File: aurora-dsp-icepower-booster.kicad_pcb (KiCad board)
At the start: 2 copper layers, 200 x 200 mm, 243 parts, among them J1 XLR_IN_1, J10 XLR3_OUT, J11 XLR3_OUT, J12 XLR3_OUT, J13 24V DC, J14 REMOTE 3.5mm, J2 XLR_IN_2, J3 XLR_IN_3, J4 XLR_IN_4, J5 XLR_IN_5, J6 XLR_IN_6, J7 XLR3_OUT, J8 XLR3_OUT, J9 XLR3_OUT, SW1 Gain CH1, SW2 Gain CH2, SW3 Gain CH3, SW4 Gain CH4, SW5 Gain CH5, SW6 Gain CH6, SW7 ALWAYS/REMOTE, U1 LM4562, U10 LM4562, U11 LM4562, U12 LM4562, U13 TEL5-2422, U14 ADP7118ARDZ-11, U15 ADP7182AUJZ-11, U2 LM4562, U3 LM4562, U4 LM4562, U5 LM4562, U6 LM4562, U7 LM4562, U8 LM4562, U9 LM4562

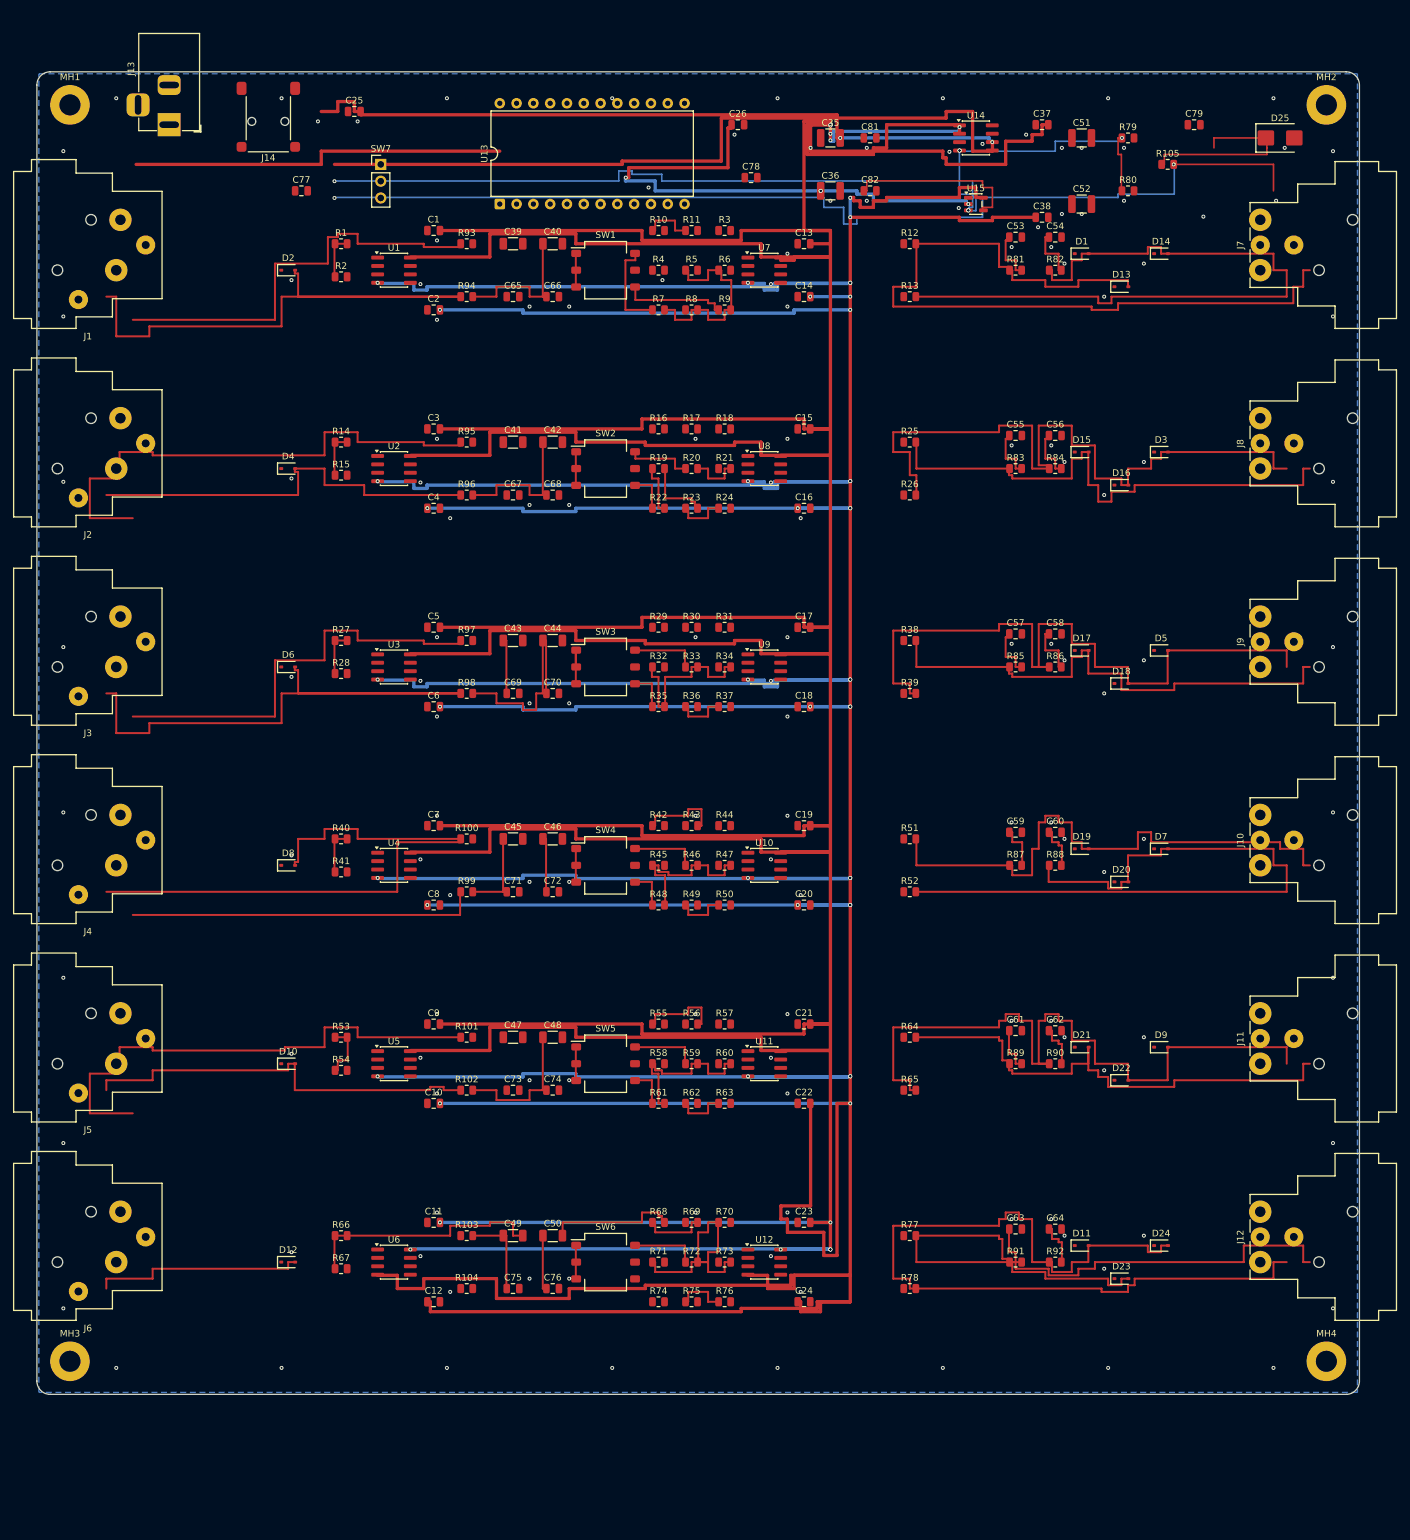
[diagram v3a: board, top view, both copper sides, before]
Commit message: SW7: Pin Header -> EG1224 SPDT Rocker Switch, Board 200x220mm, J13/SW7/J14 zentriert
- SW7 Footprint: PinHeader_1x03 -> SW_E-Switch_EG1224_SPDT_Angled
- SW7 rotiert 180°, ragt 10mm über Oberkante hinaus (Kippschalter)
- J13 (Barrel Jack) bei x=80, ragt 9mm über Oberkante
- J14 (3.5mm Remote) bei x=120, ragt 4.5mm über Oberkante
- Board von 200x200mm auf 200x220mm vergrößert (+20mm Y)
- Alle Bauteile 10mm nach unten verschoben (mehr Platz für PSU-Bereich)
- XLR IN/OUT: y=40..190 (vorher y=30..180)
- U13 (TEL5-2422) bei (70,30), PSU-Passives neu platziert
- Mounting Holes an neuen Ecken (5,5)(195,5)(5,215)(195,215)
- ERC: 805 Warnungen (Baseline, keine neuen Fehler)
- Schaltplan Footprint-Property ebenfalls aktualisiert
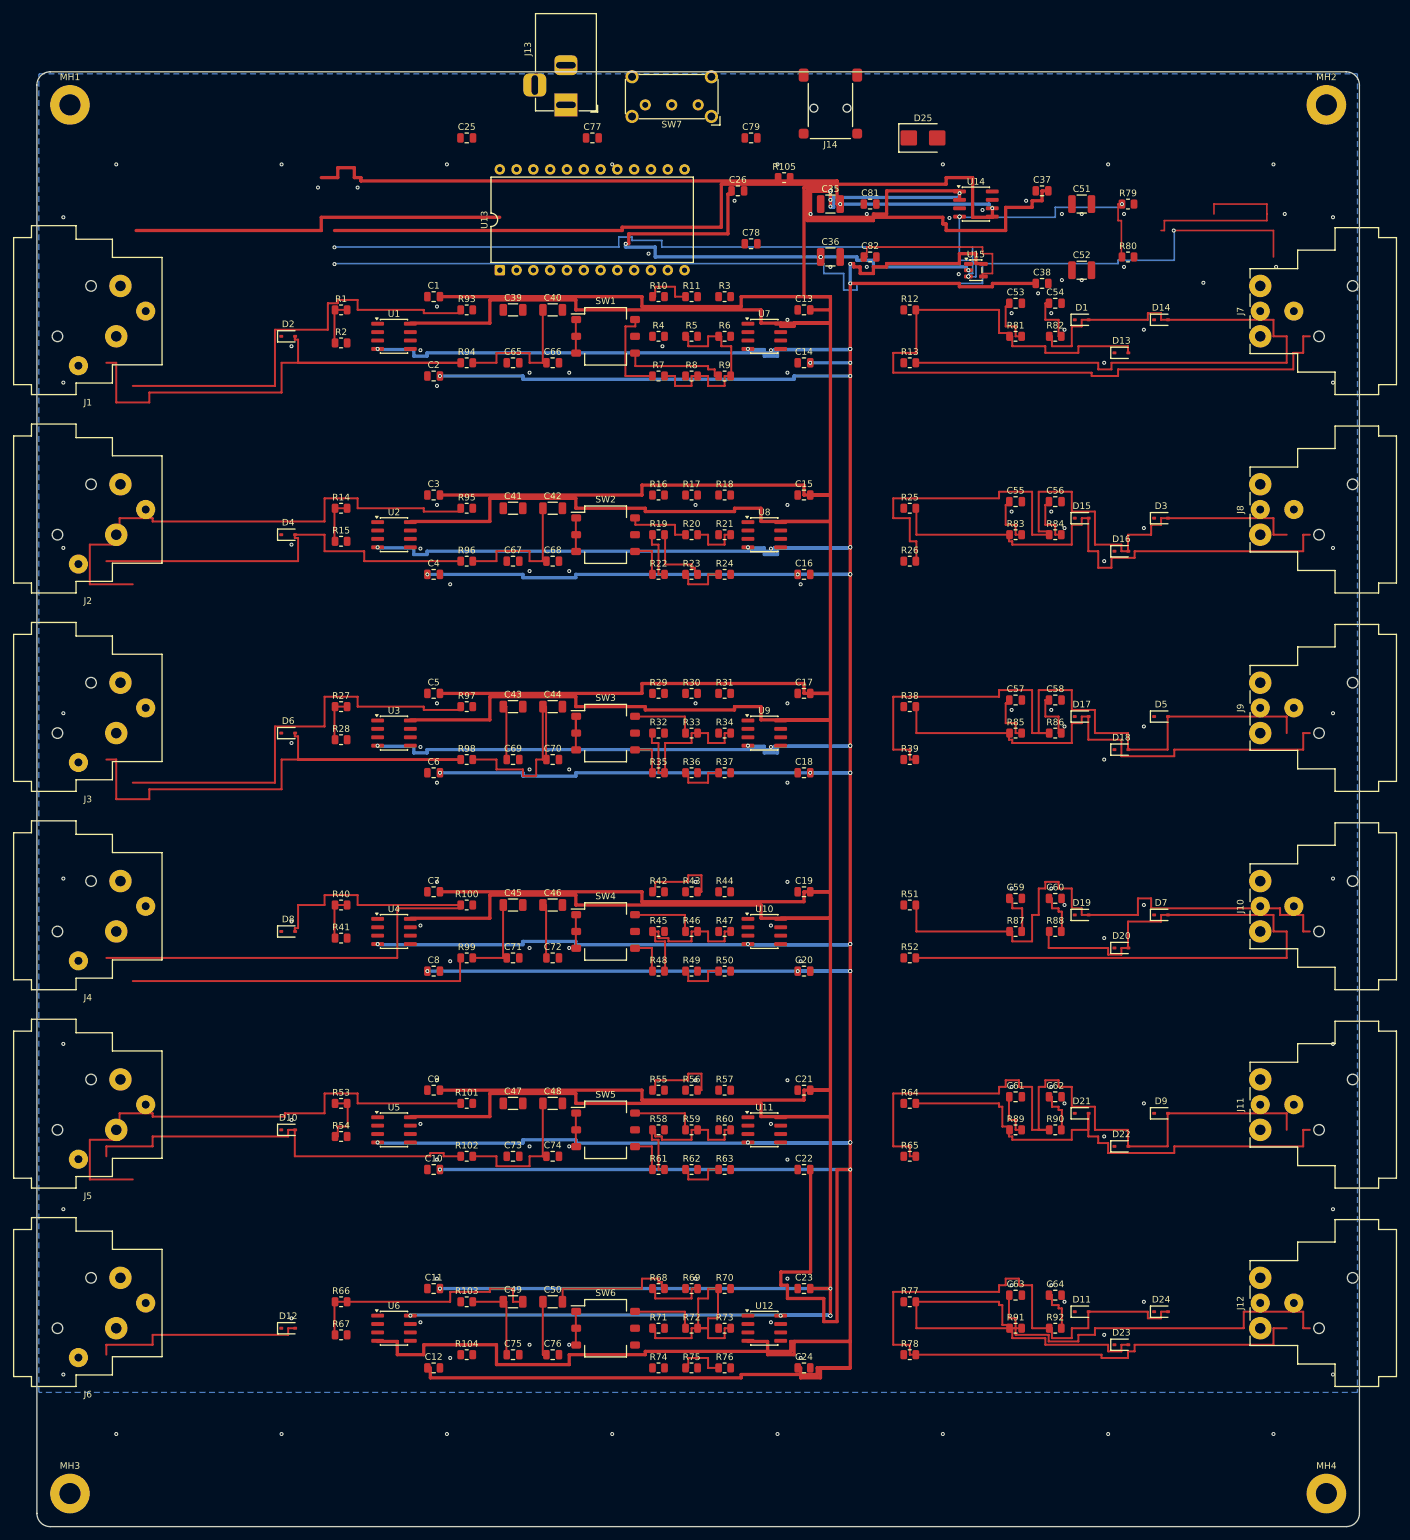
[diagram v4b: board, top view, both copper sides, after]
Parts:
- SW7: footprint Connector_PinHeader_2.54mm:PinHeader_1x03_P2.54mm_Vertical -> SW_E-Switch_EG1224_SPDT_Angled
- moved J14 85.0 mm to (120.0, 3.00)
- moved C79 67.0 mm to (108.0, 10.0)
- moved J13 60.1 mm to (80.0, 5.00)
- moved R105 58.0 mm to (113.0, 16.0)
- moved D25 54.0 mm to (134.0, 10.0)
- moved SW7 48.8 mm to (100.0, 5.00), turned to 180 degrees
- moved C77 44.7 mm to (84.0, 10.0)
- moved MH3 20.0 mm to (5.00, 215.0)
- moved MH4 20.0 mm to (195.0, 215.0)
- moved C25 17.5 mm to (65.0, 10.0)
- moved C1 10.0 mm to (60.0, 34.0)
- moved C10 10.0 mm to (60.0, 166.0)
- moved C11 10.0 mm to (60.0, 184.0)
- moved C12 10.0 mm to (60.0, 196.0)
- moved C13 10.0 mm to (116.0, 36.0)
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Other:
- board size 200 x 200 mm -> 200 x 220 mm

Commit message: PCB: Board auf 200x200mm, J13/SW7/J14 zentriert, U13+Caps verschoben
- Board-Outline von 220x220mm zurück auf 200x200mm (R=2mm)
- J13 (Barrel Jack) bei x=80, SW7 (Kippschalter) bei x=100, J14 bei x=120
  alle auf Oberkante zentriert mit Überstand für Gehäuse
- U13 (TEL5-2422) von (70,20) nach (35,18) verschoben (frei von J13/SW7)
- C25 nach (26,6), C77 nach (26,12) links neben U13
- C35 nach (130.5,3), C81 nach (130.5,11) zwischen J14 und U14
- C26 nach (107,11) unterhalb SW7
- 61 verwaiste Tracks/Vias im PSU-Bereich entfernt
- Keine Bauteil-Kollisionen, Shorts von 22 auf 18 reduziert
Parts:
- moved C79 67.0 mm to (175.0, 8.00)
- moved C77 58.0 mm to (26.0, 12.0)
- moved R105 58.0 mm to (171.0, 14.0)
- moved D25 54.0 mm to (188.0, 10.0)
- moved C25 39.2 mm to (26.0, 6.00)
- moved U13 37.0 mm to (35.0, 18.0)
- moved MH3 20.0 mm to (5.00, 195.0)
- moved MH4 20.0 mm to (195.0, 195.0)
- moved C35 20.0 mm to (130.5, 3.00)
- moved C81 10.1 mm to (130.5, 11.0)
- moved C1 10.0 mm to (60.0, 24.0)
- moved C10 10.0 mm to (60.0, 156.0)
- moved C11 10.0 mm to (60.0, 174.0)
- moved C12 10.0 mm to (60.0, 186.0)
- moved C13 10.0 mm to (116.0, 26.0)
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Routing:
- net /+12V: track 224.0 -> 45.5 mm, vias 2 -> 1
- net /V+: track 1143.0 -> 1024.0 mm, vias 15 -> 8
- net /+24V_IN: track 57.0 -> 0.00 mm
- net /EN_CTRL: track 152.5 -> 106.0 mm
- net /V-: track 1256.0 -> 1214.0 mm
- net /GND: track 0.00 -> 15.0 mm, vias 138 -> 131
- net /CH1_OUT_COLD: track 173.0 -> 162.5 mm
- net /CH1_EMI_COLD: track 22.5 -> 14.5 mm
- net /-12V: track 80.0 -> 73.0 mm, vias 4 -> 3
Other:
- board size 200 x 220 mm -> 200 x 200 mm

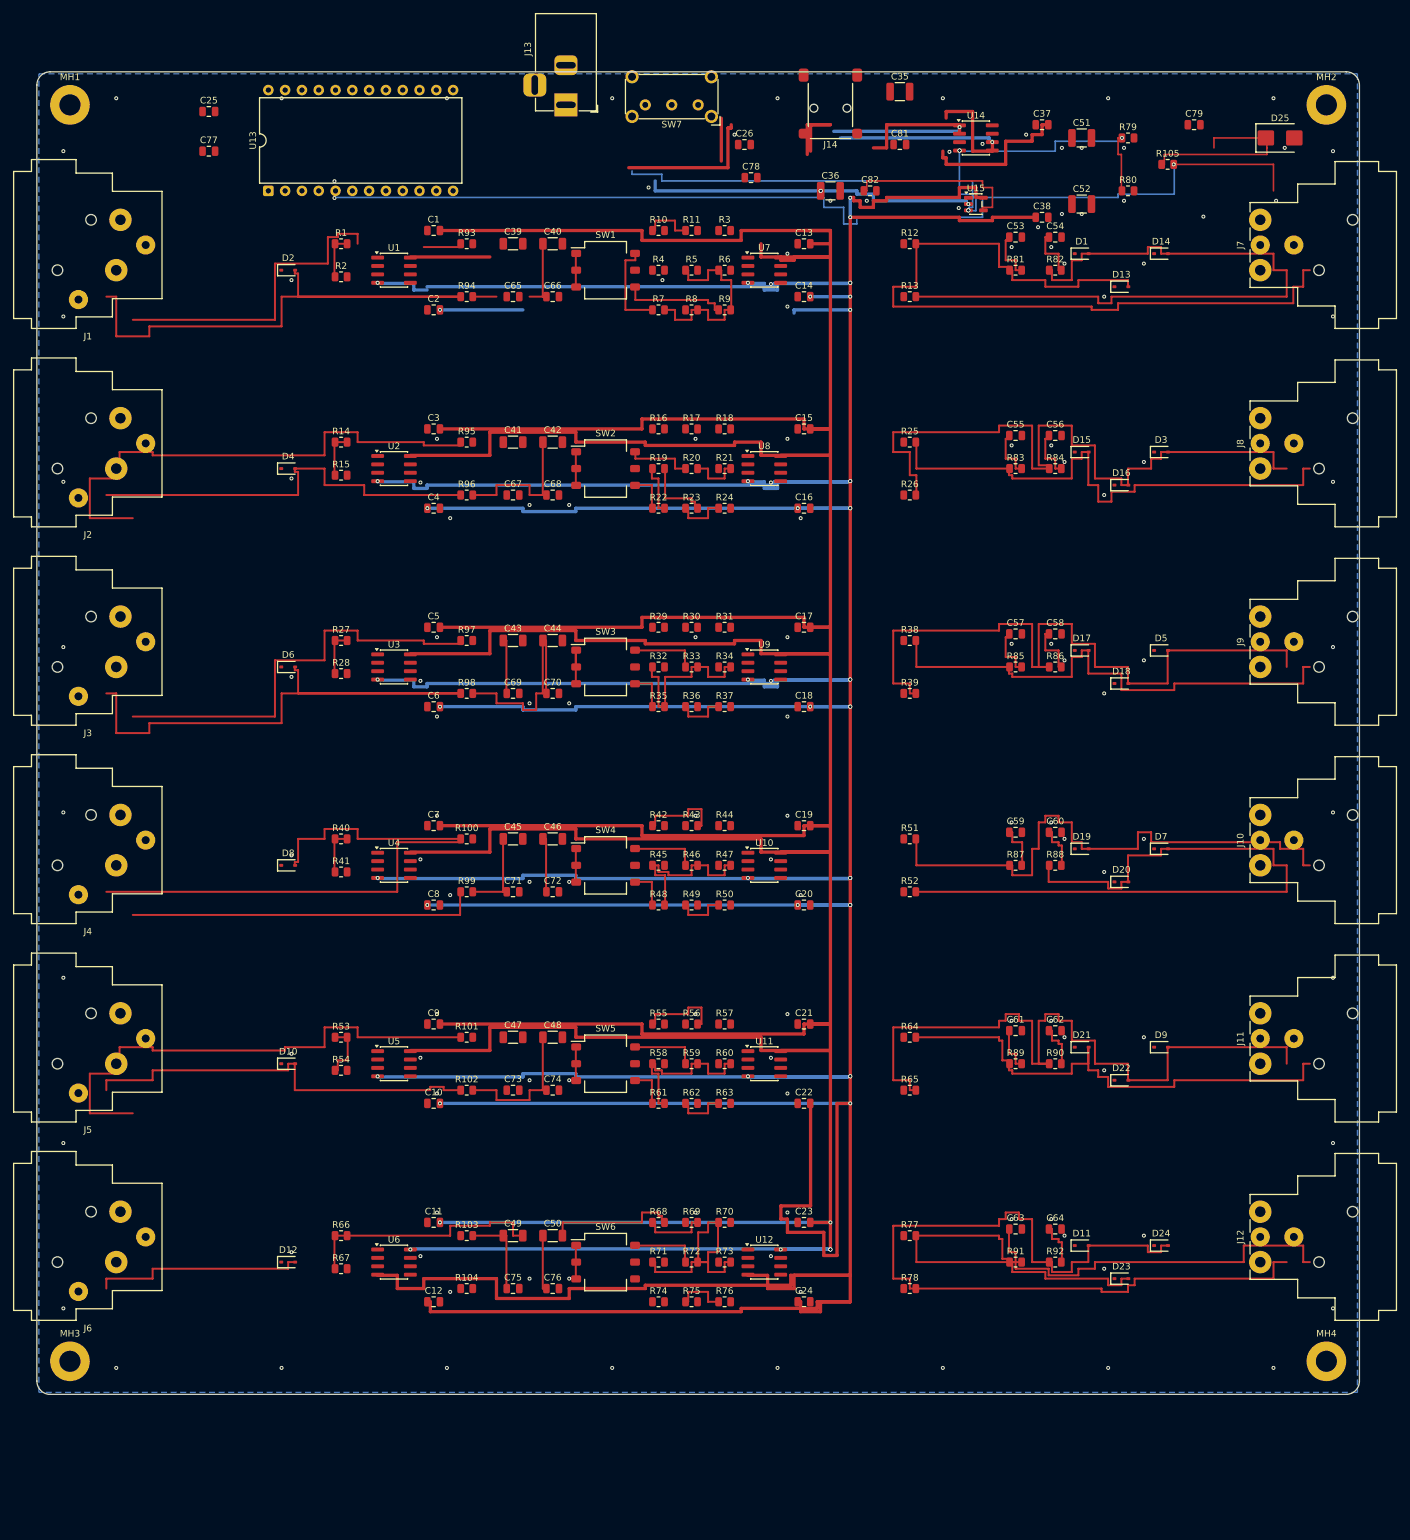
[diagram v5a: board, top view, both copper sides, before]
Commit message: PCB: Alle Tracks/Vias gelöscht + Speaker-Netzklasse hinzugefügt
- 1043 Tracks + 194 Vias entfernt (clean slate für Routing-Neubeginn)
- Speaker-Netzklasse: 1.5mm Track, 0.8mm Via, 0.3mm Clearance
- CHx_EMI_HOT/COLD von Audio_Input auf Speaker umgestellt
- DRC: 0 Shorts, 0 Dangles, 479 Unconnected (erwartungsgemäß)
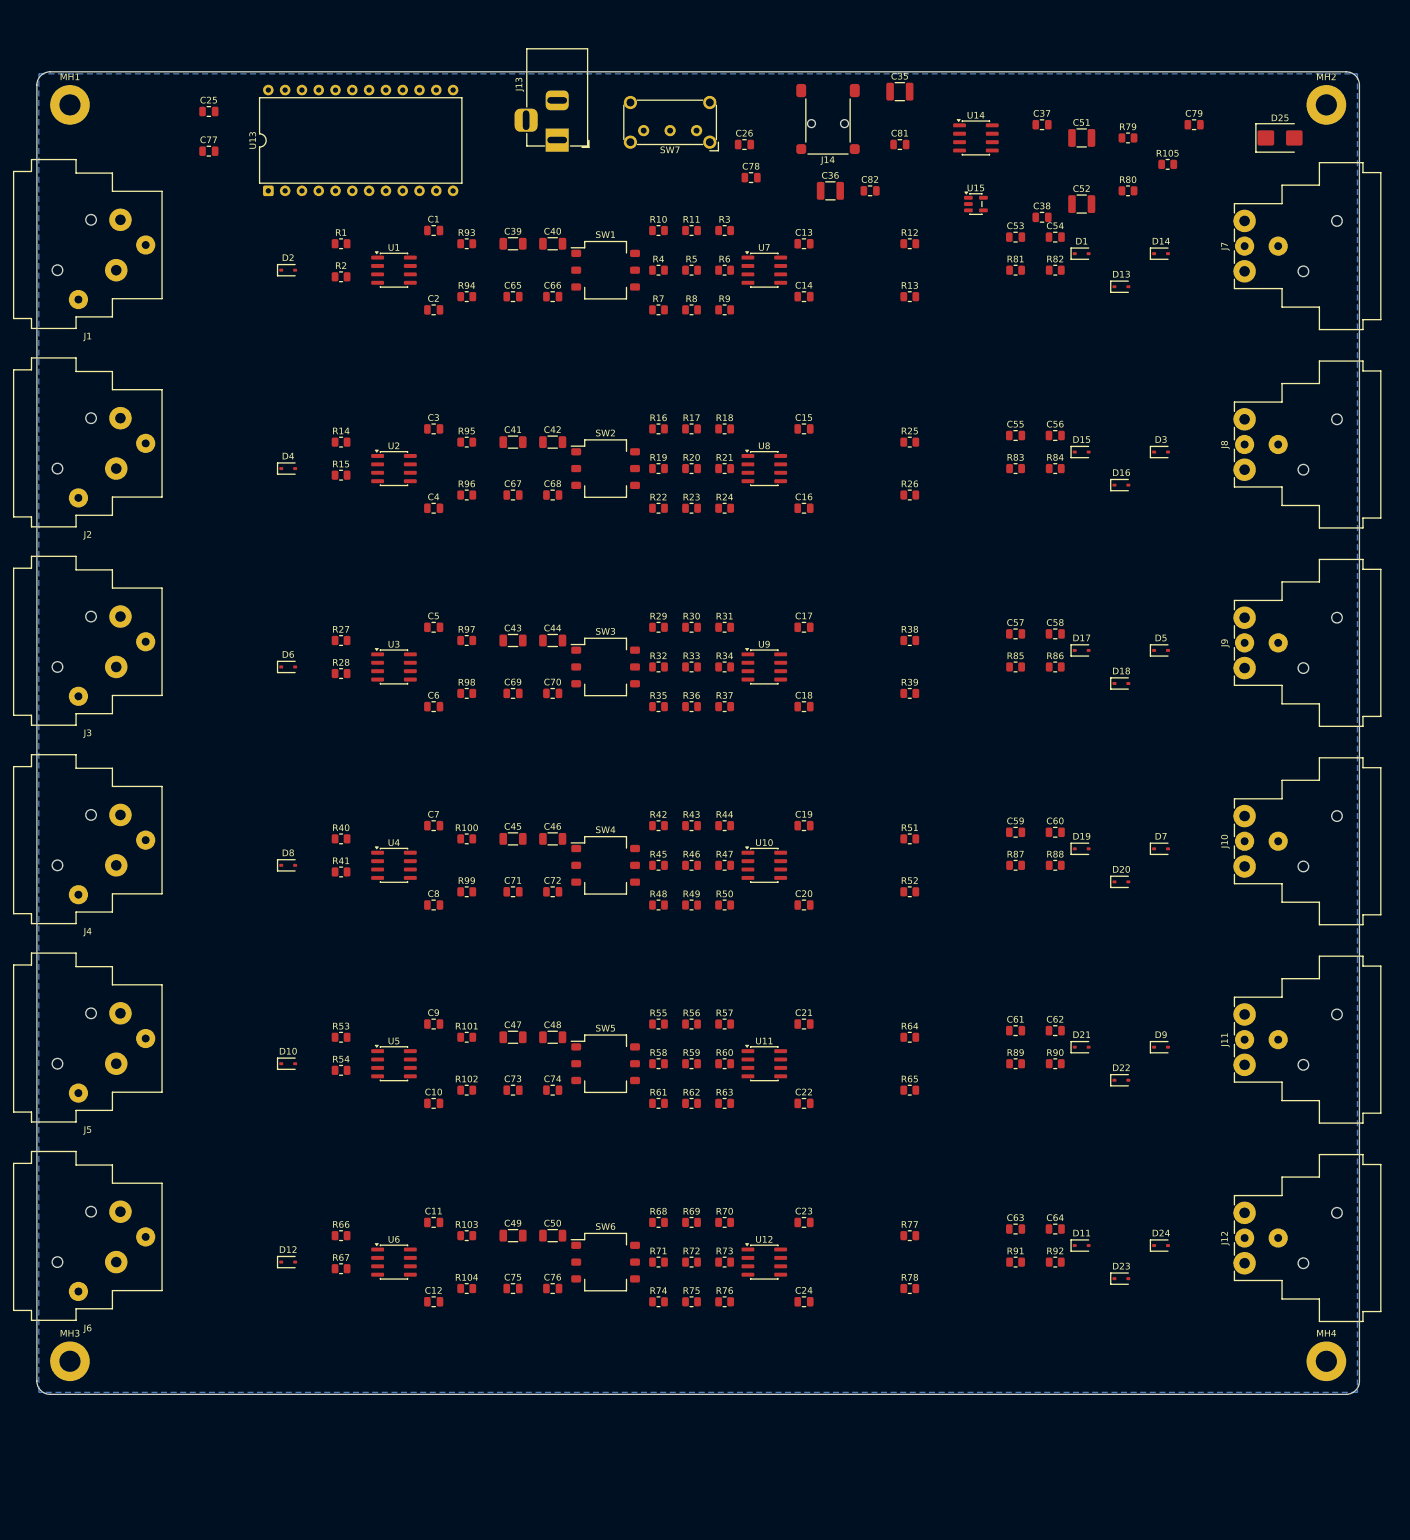
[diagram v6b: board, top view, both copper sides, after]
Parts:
- moved J13 5.48 mm to (78.7, 10.3)
- moved SW7 3.90 mm to (99.8, 8.89)
- moved J10 2.37 mm to (182.6, 120.2)
- moved J7 2.37 mm to (182.6, 30.2)
- moved J8 2.37 mm to (182.6, 60.2)
- moved J9 2.37 mm to (182.6, 90.2)
- moved J11 2.37 mm to (182.6, 150.2)
- moved J12 2.37 mm to (182.6, 180.2)
- moved J14 2.36 mm to (119.6, 5.33)
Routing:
- net /V-: track 1214.0 -> 0.00 mm, vias 43 -> 0
- net /V+: track 1024.0 -> 0.00 mm, vias 8 -> 0
- net /CH5_OUT_COLD: track 188.0 -> 0.00 mm
- net /CH2_OUT_COLD: track 185.0 -> 0.00 mm
- net /CH3_OUT_COLD: track 171.0 -> 0.00 mm
- net /CH1_OUT_COLD: track 162.5 -> 0.00 mm
- net /CH4_OUT_COLD: track 161.0 -> 0.00 mm
- net /REMOTE_FILT: track 159.0 -> 0.00 mm, vias 2 -> 0
- net /CH6_OUT_COLD: track 132.5 -> 0.00 mm
- net /CH1_OUT_HOT: track 123.0 -> 0.00 mm
- net /CH6_OUT_HOT: track 113.0 -> 0.00 mm
- net /EN_CTRL: track 106.0 -> 0.00 mm, vias 6 -> 0
- net /CH3_COLD_RAW: track 94.5 -> 0.00 mm
- net /CH1_COLD_RAW: track 94.5 -> 0.00 mm
- net /CH4_COLD_RAW: track 93.5 -> 0.00 mm
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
